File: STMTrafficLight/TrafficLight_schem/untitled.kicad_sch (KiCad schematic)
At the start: 66 parts, among them SW1 SW_Push, SW2 SW_Push, SW3 SW_Push, SW4 SW_Push, U1 74HC595D, U2 74HC595D, U3 74HC595D

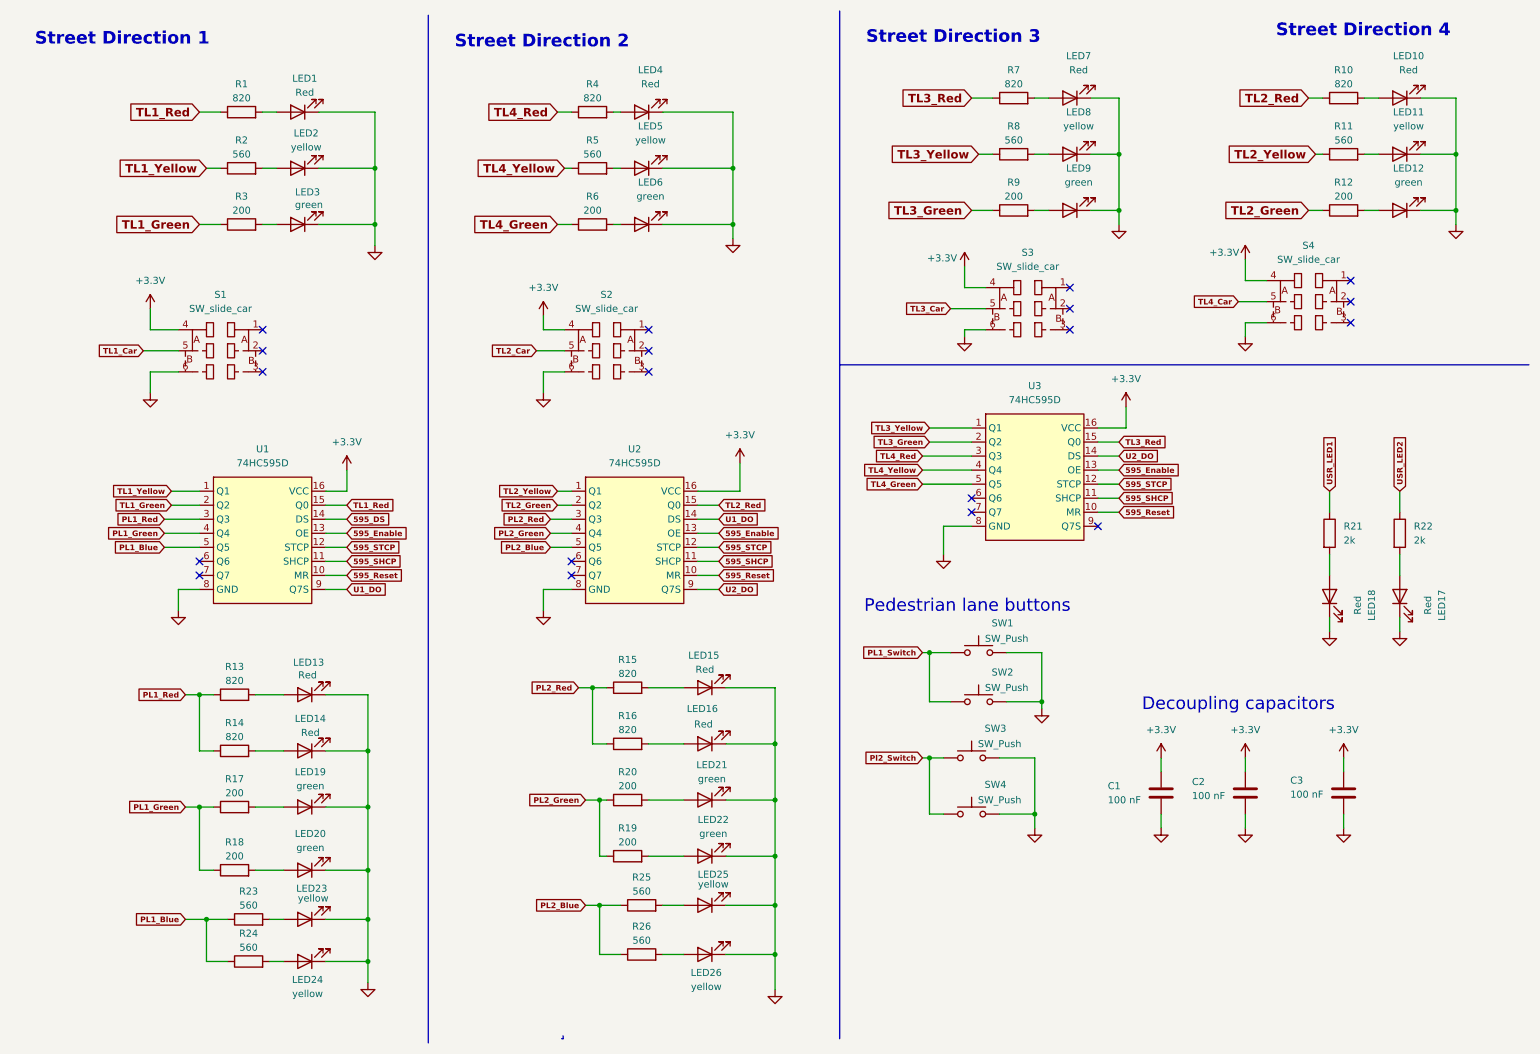
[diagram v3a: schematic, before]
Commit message: continued on the traffic light shield
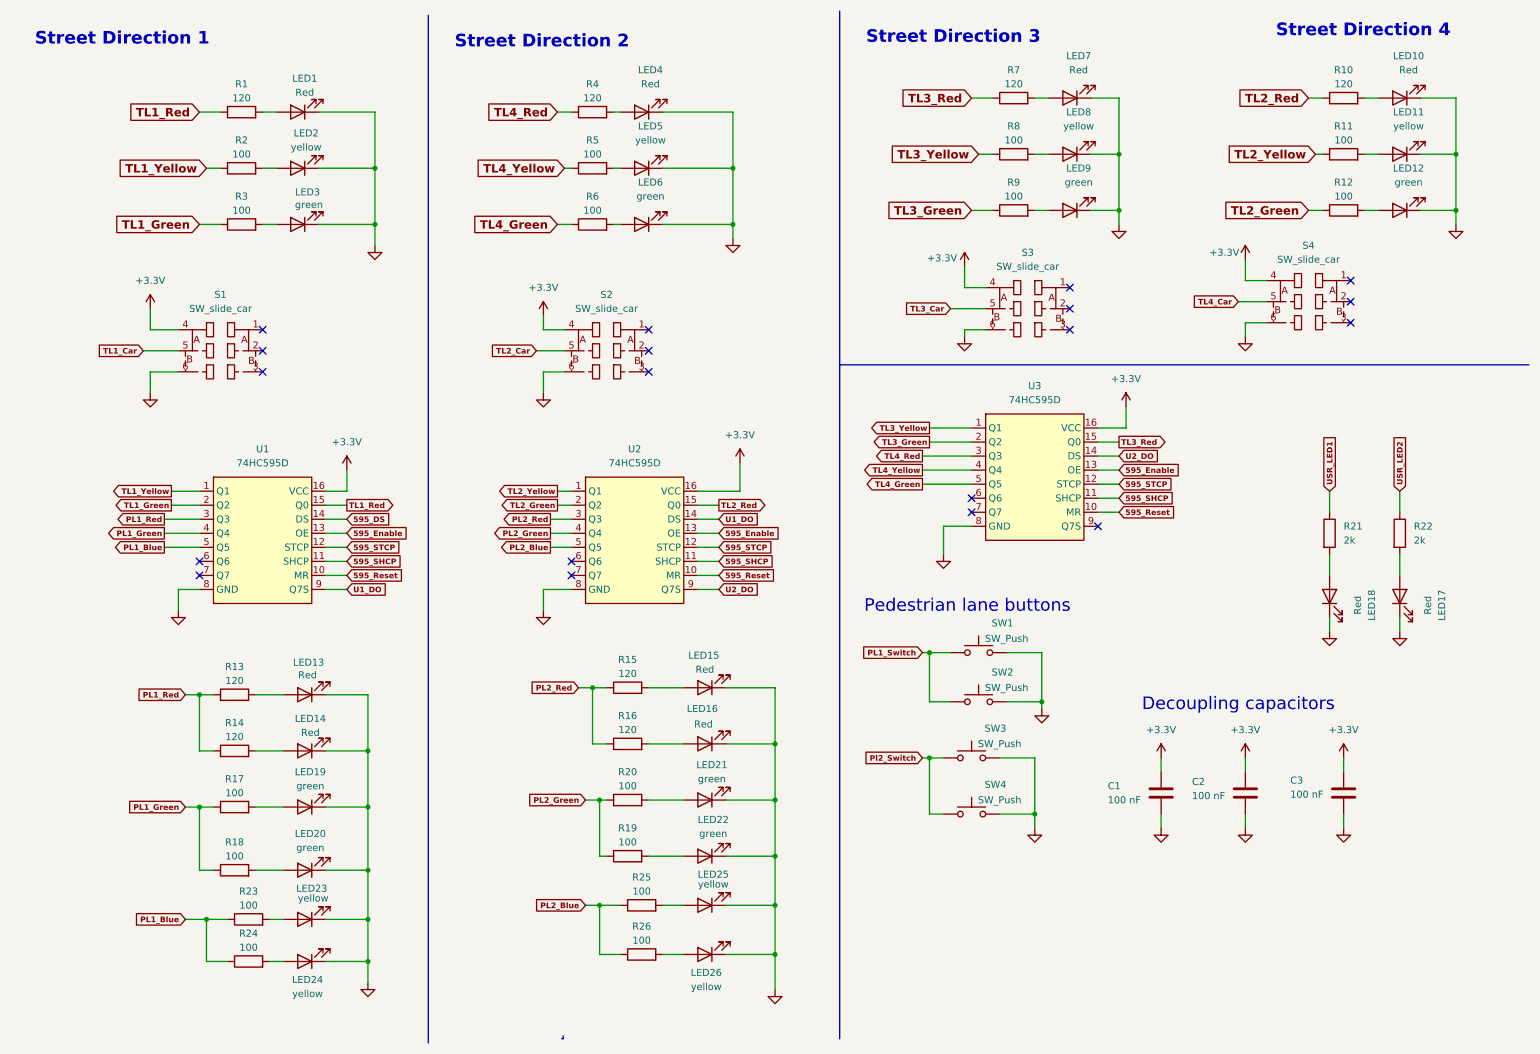
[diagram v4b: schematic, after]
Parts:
- LED1, LED10, LED13, LED14, LED15, LED16, LED17, LED18, LED4, LED7: Distributor link 1 https://jlcpcb.com/partdetail/85425-NCD0805R1/C84256 -> https://jlcpcb.com/partdetail/YongyuPhotoelectric-SZYY0805R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; Distributor link 2 https://www.lcsc.com/product-detail/C84256.html -> https://www.lcsc.com/product-detail/C434431.html; LCSC C84256 -> C434431; Manufacturer Foshan NationStar Optoelectronics -> Yongyu Photoelectric; Manufacturer part number NCD0805R1 -> Yongyu Photoelectric
- LED11, LED2, LED23, LED24, LED25, LED26, LED5, LED8: Distributor Link 2 https://jlcpcb.com/partdetail/Hubei_KENTOElec-KT0805Y/C2296 -> https://jlcpcb.com/partdetail/YongyuPhotoelectric-SZYY0805Y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; Distributor link  2 (none) -> https://www.lcsc.com/product-detail/C434436.html; LCSC C2296 -> C434436; Manufacturer Hubei KENTO Elec -> Yongyu Photoelectric; Manufacturer part number KT-0805Y -> SZYY0805Y
- LED12, LED19, LED20, LED21, LED22, LED3, LED6, LED9: Distributor Link 2 https://www.lcsc.com/product-detail/C2297.html -> https://jlcpcb.com/partdetail/YongyuPhotoelectric-SZYY0805Y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
- R1, R10, R13, R14, R15, R16, R4, R7: value 820 -> 120; footprint Resistor_SMD:R_0603_1608Metric -> Resistor_SMD:R_0805_2012Metric; Distributor link 1 https://www.mouser.se/ProductDetail/Royalohm/0603WAF8200T5E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 -> https://www.mouser.se/ProductDetail/Royalohm/0805W8F1200T5E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; Distributor link 2 https://www.tme.eu/en/details/0603waf8200t5e/smd-resistors/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 -> https://www.lcsc.com/product-detail/C17437.html; LCSC C23253 -> C17437; Manufacture Part number 0603WAF8200T5E -> 0805W8F1200T5E
- R11, R2, R23, R24, R25, R26, R5, R8: value 560 -> 100; Distributor link 1 https://www.mouser.se/ProductDetail/Royalohm/0603WAF5600T5E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 -> https://www.mouser.se/ProductDetail/Royalohm/0805W8J0100T5E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; Distributor link 2 https://www.lcsc.com/product-detail/C23204.html -> https://www.lcsc.com/product-detail/C17408.html; LCSC C23204 -> C17408; Manufacture Part number 0603WAF5600T5E -> 0805W8F1000T5E
- R12, R17, R18, R19, R20, R3, R6, R9: value 200 -> 100; Distributor link 1 https://www.mouser.se/ProductDetail/Royalohm/0603WAF2000T5E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 -> https://www.mouser.se/ProductDetail/Royalohm/0805W8J0100T5E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; Distributor link 2 https://www.tme.eu/en/details/0603waf2000t5e/smd-resistors/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 -> https://www.lcsc.com/product-detail/C17408.html; LCSC C8218 -> C17408; Manufacture Part number 0603WAF2000T5E -> 0805W8F1000T5E
- R21, R22: Distributor link 2 https://www.lcsc.com/product-detail/C22975.html -> (none)

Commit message: continued on the traffic light shield
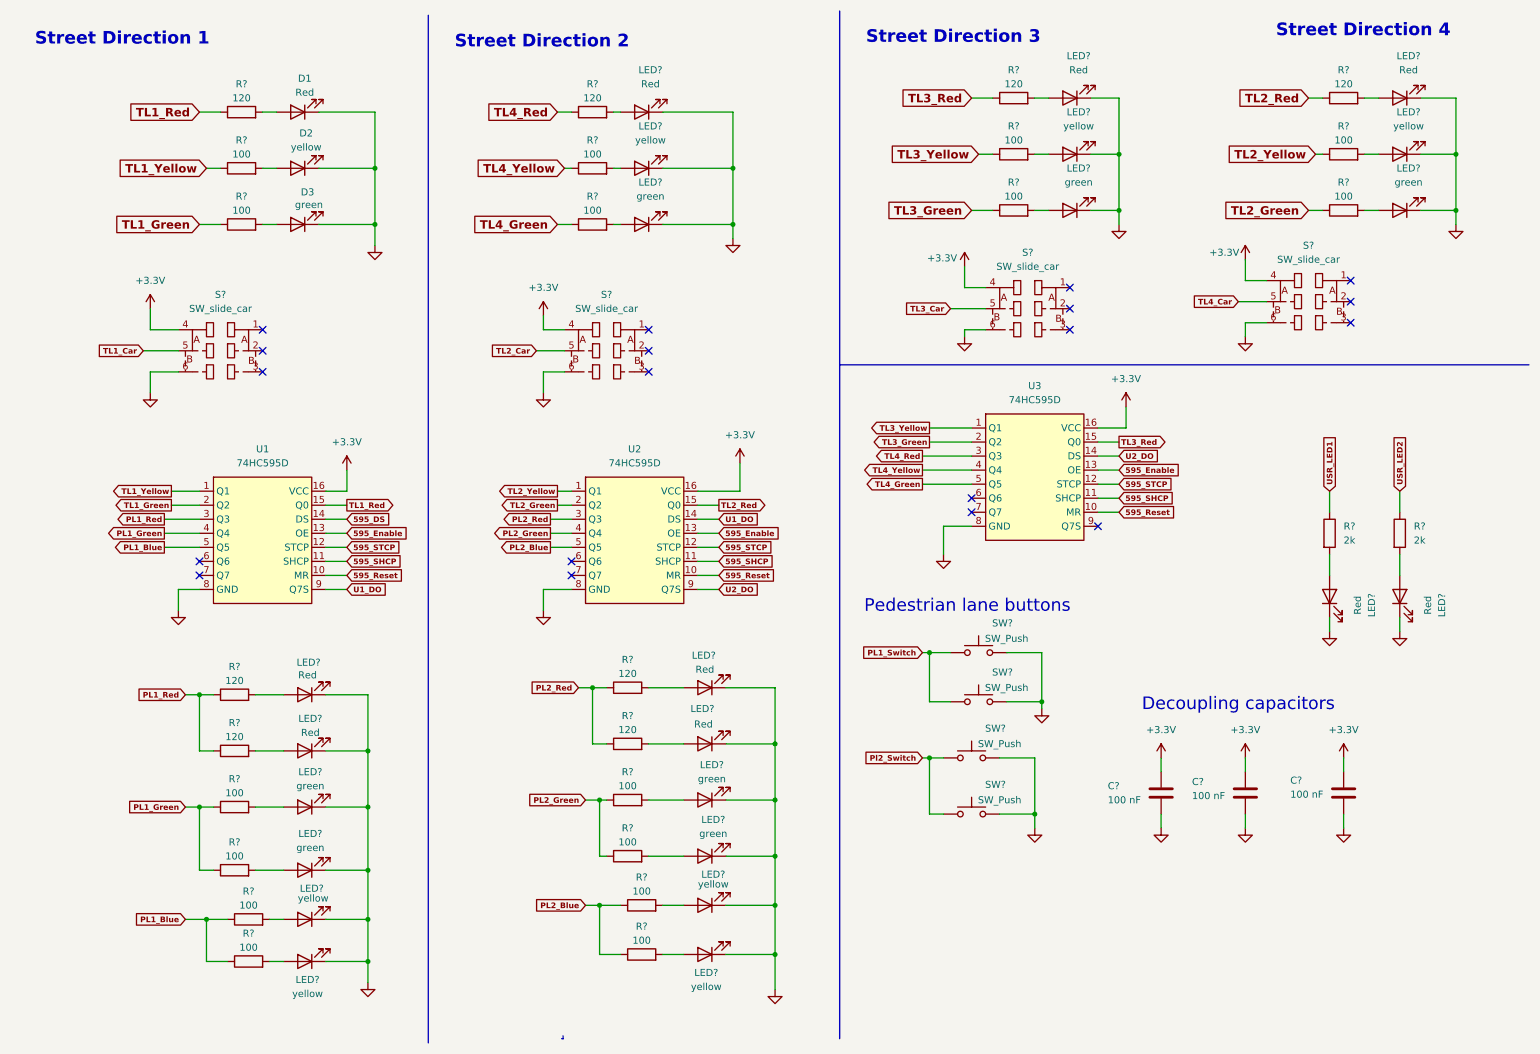
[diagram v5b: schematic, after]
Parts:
- renumbered C1 to C?, C2 to C?, C3 to C?, LED1 to D1, LED2 to D2, LED3 to D3, LED15 to LED?, LED14 to LED?, LED10 to LED?, LED22 to LED?, LED26 to LED?, LED8 to LED?, LED5 to LED?, LED6 to LED?, LED23 to LED?, LED19 to LED?, LED18 to LED?, LED24 to LED?, LED20 to LED?, LED13 to LED?, LED12 to LED?, LED17 to LED?, LED21 to LED?, LED25 to LED?, LED16 to LED?, LED9 to LED?, LED4 to LED?, LED11 to LED?, LED7 to LED?, R23 to R?, R19 to R?, R9 to R?, R24 to R?, R25 to R?, R22 to R?, R18 to R?, R2 to R?, R7 to R?, R21 to R?, R11 to R?, R20 to R?, R1 to R?, R14 to R?, R5 to R?, R26 to R?, R6 to R?, R10 to R?, R12 to R?, R8 to R?, R15 to R?, R16 to R?, R17 to R?, R13 to R?, R4 to R?, R3 to R?, S2 to S?, S4 to S?, S1 to S?, S3 to S?, SW4 to SW?, SW2 to SW?, SW1 to SW?, SW3 to SW?
